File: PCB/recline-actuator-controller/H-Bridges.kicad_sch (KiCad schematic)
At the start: 0 parts

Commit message: Recline Actuator Control
Recline controller board schematic and Recline actuator board schematics. Actuator control board schematic 90% complete.
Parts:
- added C24, C25: UUQ1H470MCL1GS, AVR-KiCAD-Lib-Capacitors:CP_Elec_8x10, symbol AVR-KiCAD-Lib-Capacitors:UUQ1H470MCL1GS
- added C26, C27: CL21B104KBFNNNE, AVR-KiCAD-Lib-Capacitors:C0805, symbol AVR-KiCAD-Lib-Capacitors:CL21B104KBFNNNE
- added C28, C29: C0402C333K4REC7867, AVR-KiCAD-Lib-Capacitors:C0402, symbol AVR-KiCAD-Lib-Capacitors:C0402C333K4REC7867
- added D13, D15: LTST-C194KGKT, AVR-KiCAD-Lib-Diodes:LED0603, symbol AVR-KiCAD-Lib-Diodes:LTST-C194KGKT
- added D14, D16: LTST-C194TBKT, AVR-KiCAD-Lib-Diodes:LED0603, symbol AVR-KiCAD-Lib-Diodes:LTST-C194TBKT
- added J5, J6: 1757242, AVR-KiCAD-Lib-Connectors:PhoenixContact_MSTBA-G_02x5.08mm_Angled, symbol AVR-KiCAD-Lib-Connectors:1757242
- added Q6, Q7: AOD4132, AVR-KiCAD-Lib-Transistors:TO-252-2, symbol AVR-KiCAD-Lib-Transistors:AOD4132
- added R28, R29: RC0805FR-074K7L, AVR-KiCAD-Lib-Resistors:R0805, symbol AVR-KiCAD-Lib-Resistors:RC0805FR-074K7L
- added R30, R32, R33, R34, R35, R36, R37, R38, R39, R40: RC0402FR-071KL, AVR-KiCAD-Lib-Resistors:R0402, symbol AVR-KiCAD-Lib-Resistors:RC0402FR-071KL
- added R31, R41, R42, R43: RC0402FR-0710KL, AVR-KiCAD-Lib-Resistors:R0402, symbol AVR-KiCAD-Lib-Resistors:RC0402FR-0710KL
- added R44, R45: RC0402FR-074K7L, AVR-KiCAD-Lib-Resistors:R0402, symbol AVR-KiCAD-Lib-Resistors:RC0402FR-074K7L
- added U4, U5: VNH5019ATR-E, AVR-KiCAD-Lib-ICs:IC_VNH5019ATR-E, symbol AVR-KiCAD-Lib-ICs:VNH5019ATR-E
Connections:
- new net: R36.1, U5.4 (INA)
- new net: R30.1, R44.1, U4.5 (ENA/DIAGA), U4.9 (ENB/DIAGB)
- new net: R33.1, U4.10 (INB)
- new net: Q6.1 (G), U4.11 (CP)
- new net: R32.1, U4.4 (INA)
- new net: R34.1, U4.7 (PWM)
- new net: R31.1, R39.2, U4.8 (CS)
- new net: R35.1, R45.1, U5.5 (ENA/DIAGA), U5.9 (ENB/DIAGB)
- new net: R37.1, U5.10 (INB)
- new net: Q7.1 (G), U5.11 (CP)
- new net: R38.1, U5.7 (PWM)
- new net: R40.2, R41.1, U5.8 (CS)
- new net: D15.1, D16.2, R29.1
- new net: D13.1, D14.2, R28.1
- new net +24V: Q6.2 (D), Q7.2 (D), U4.12 (VBAT), U5.12 (VBAT)
- new net +3.3V: R44.2, R45.2
- new net GND: C24.2, C25.2, C26.1, C27.1, C28.1, C29.1, R39.1, R40.1, R42.1, R43.1, U4.18 (GNDB), U4.19 (GNDB__1), U4.20 (GNDB__2), U4.26 (GNDA), U4.27 (GNDA__1), U4.28 (GNDA__2), U5.18 (GNDB), U5.19 (GNDB__1), U5.20 (GNDB__2), U5.26 (GNDA), U5.27 (GNDA__1), U5.28 (GNDA__2)
- new net M1CS: C28.2, R31.2
- new net M1ENA/B: R30.2
- new net M1INA: R32.2
- new net M1INB: R33.2
- new net M1OUTA: D13.2, D14.1, J5.1, U4.1 (OUTA), U4.25 (OUTA__1), U4.30 (OUTA__2), U4.HS2 (OUTA__3)
- new net M1OUTB: J5.2, R28.2, U4.15 (OUTB), U4.16 (OUTB__1), U4.21 (OUTB__2), U4.HS3 (OUTB__3)
- new net M1PWM: R34.2, R42.2
- new net M2CS: C29.2, R41.2
- new net M2ENA/B: R35.2
- new net M2INA: R36.2
- new net M2INB: R37.2
- new net M2OUTA: D15.2, D16.1, J6.1, U5.1 (OUTA), U5.25 (OUTA__1), U5.30 (OUTA__2), U5.HS2 (OUTA__3)
- new net M2OUTB: J6.2, R29.2, U5.15 (OUTB), U5.16 (OUTB__1), U5.21 (OUTB__2), U5.HS3 (OUTB__3)
- new net M2PWM: R38.2, R43.2
- new net VMOT1: C24.1, C26.2, Q6.3 (S), U4.13 (VCC__1), U4.23 (VCC__2), U4.3 (VCC), U4.HS1 (VCC__3)
- new net VMOT2: C25.1, C27.2, Q7.3 (S), U5.13 (VCC__1), U5.23 (VCC__2), U5.3 (VCC), U5.HS1 (VCC__3)
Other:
- note added: "Motor H-Bridges"

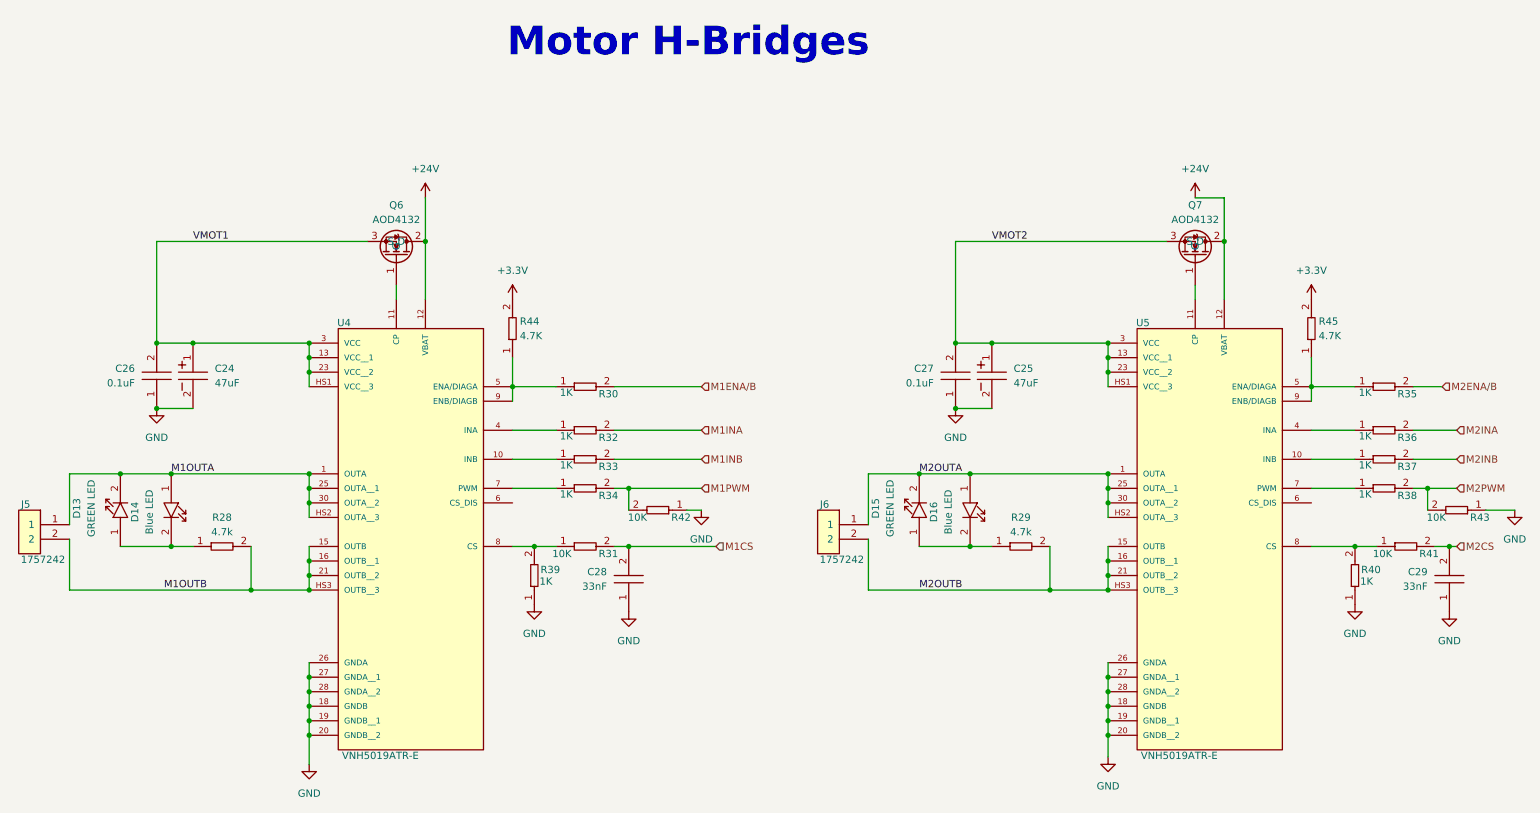
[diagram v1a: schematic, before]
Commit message: Actuator Control Board  MOSFET
Swapped Actuator control board MOSFET over to a more thermally efficient part
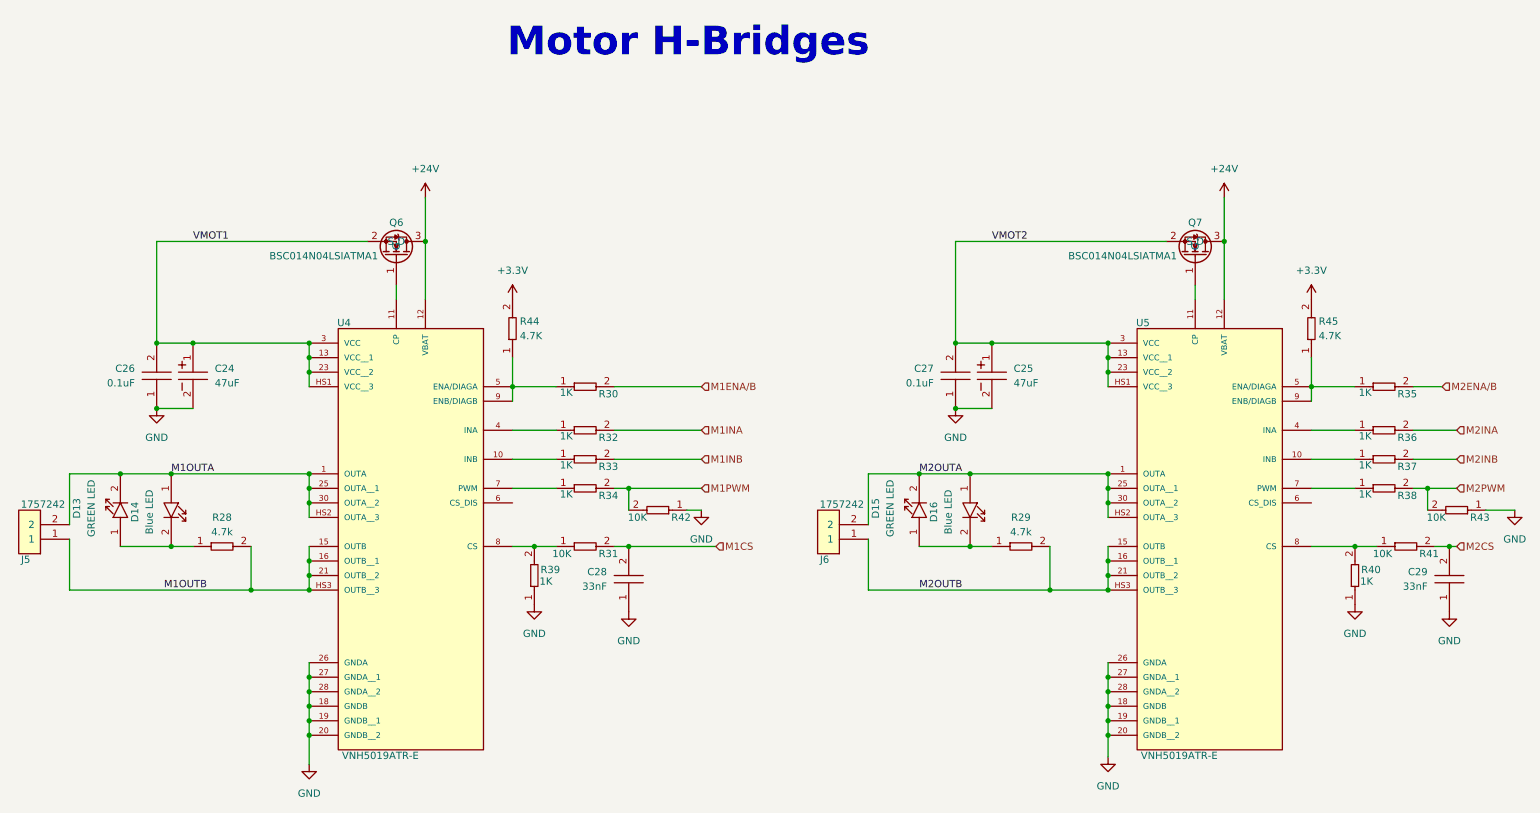
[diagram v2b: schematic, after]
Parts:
- removed Q6, Q7: AOD4132, AVR-KiCAD-Lib-Transistors:TO-252-2, symbol AVR-KiCAD-Lib-Transistors:AOD4132
- added Q6, Q7: BSC014N04LSIATMA1, AVR-KiCAD-Lib-Transistors:PG-TDSON-8_INF, symbol AVR-KiCAD-Lib-Transistors:BSC014N04LSIATMA1
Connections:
- net +24V: now also Q6.3 (D), Q7.3 (D)
- net M1OUTA: now also J5.2; no longer J5.1
- net M1OUTB: now also J5.1; no longer J5.2
- net M2OUTA: now also J6.2; no longer J6.1
- net M2OUTB: now also J6.1; no longer J6.2
- net VMOT1: now also Q6.2 (S)
- net VMOT2: now also Q7.2 (S)
- net at U4.11 (CP): now also Q6.1 (G)
- net at U5.11 (CP): now also Q7.1 (G)
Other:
- moved on the sheet: J5, J6
